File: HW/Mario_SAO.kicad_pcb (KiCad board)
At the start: 2 copper layers, 57.5 x 67.5 mm, 11 parts, among them X1 Badgelife_sao_connector_v169b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

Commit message: routed LEDs and ground pour
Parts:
- moved D3 68.9 mm to (119.5, 122.2), turned to 90 degrees
- moved R2 65.8 mm to (109.2, 107.0)
- moved D4 47.2 mm to (115.0, 111.2), turned to 135 degrees
- moved D2 0.15 mm to (99.9, 107.5)
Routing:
- net Net-(D3-Pad2): track 0.00 -> 18.6 mm
- net VCC: track 10.5 -> 26.6 mm
- net Net-(D1-Pad2): track 3.63 -> 16.9 mm
- added copper zone on B.Cu, net GND

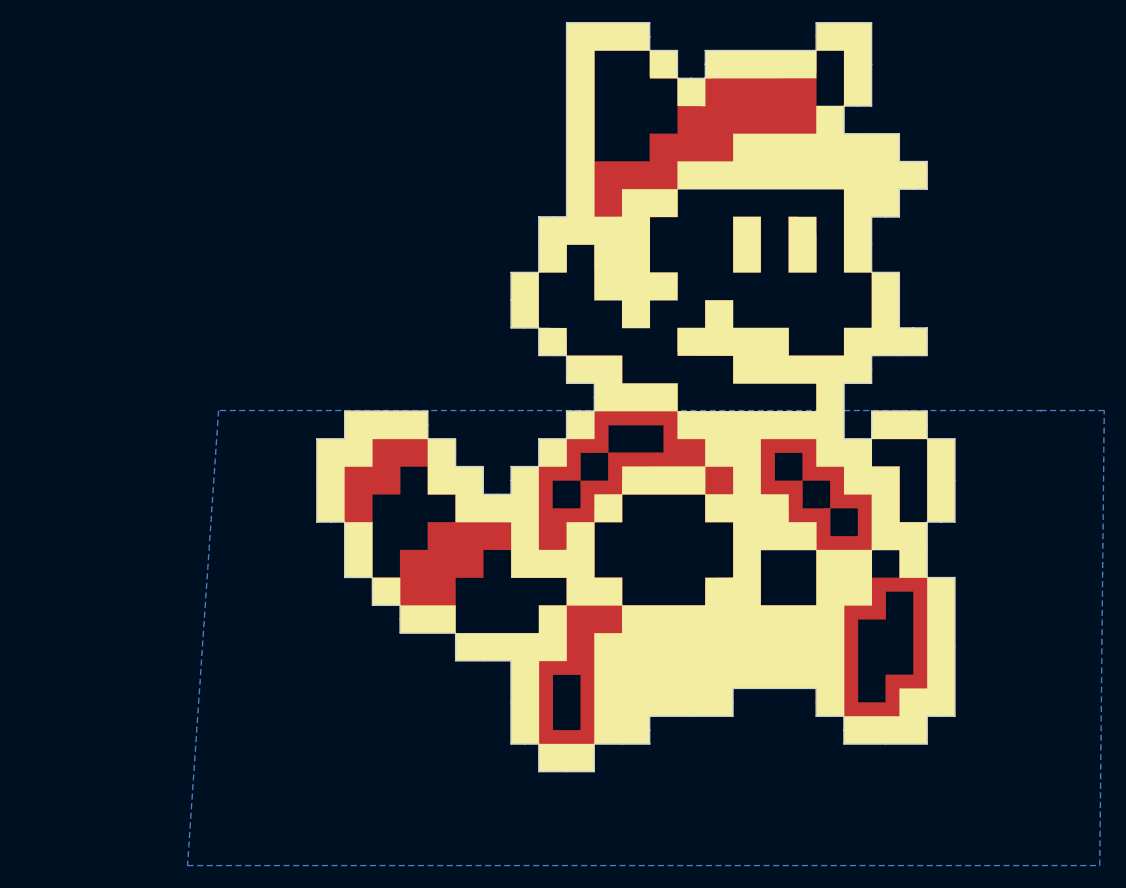
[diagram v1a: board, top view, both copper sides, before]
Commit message: Finished F.Cu, Got B.Cu added.
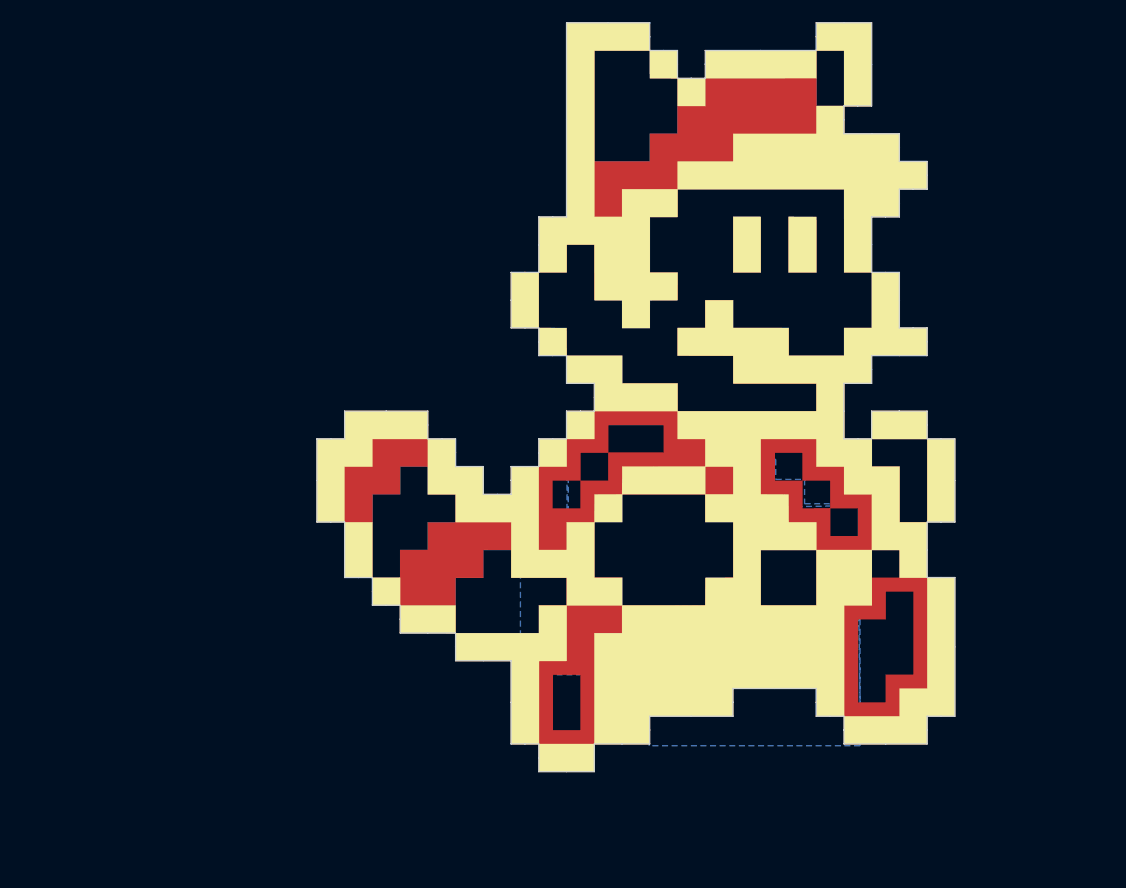
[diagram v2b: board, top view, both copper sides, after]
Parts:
- added G***: LOGO, Mario_SAO:B.Cu_g4148, F.Cu at (101.0, 100.0)
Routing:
- added copper zone on F.Cu, net GND

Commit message: Added silk art
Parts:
- added G***: LOGO, Mario_SAO:B.Silk_g4152, F.Cu at (101.0, 100.0)
